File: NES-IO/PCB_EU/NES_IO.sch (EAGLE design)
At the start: 63 parts, among them IC1 74HC125D, J1.1 MY_JUMPER, J1.2 MY_JUMPER, J2.2 10k, J4.C MY_JUMPER, J4.V MY_JUMPER, J6 MY_JUMPER, J7 MY_JUMPER

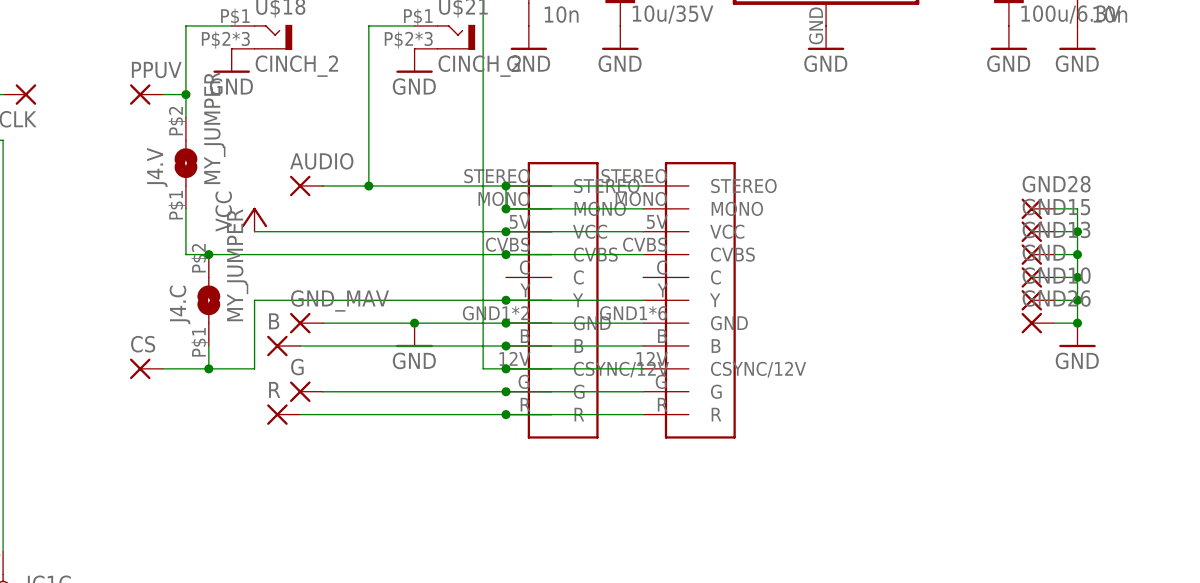
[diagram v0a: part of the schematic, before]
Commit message: Common design for MultiAV (from SNES or GC) and FR-NES-RGB jack
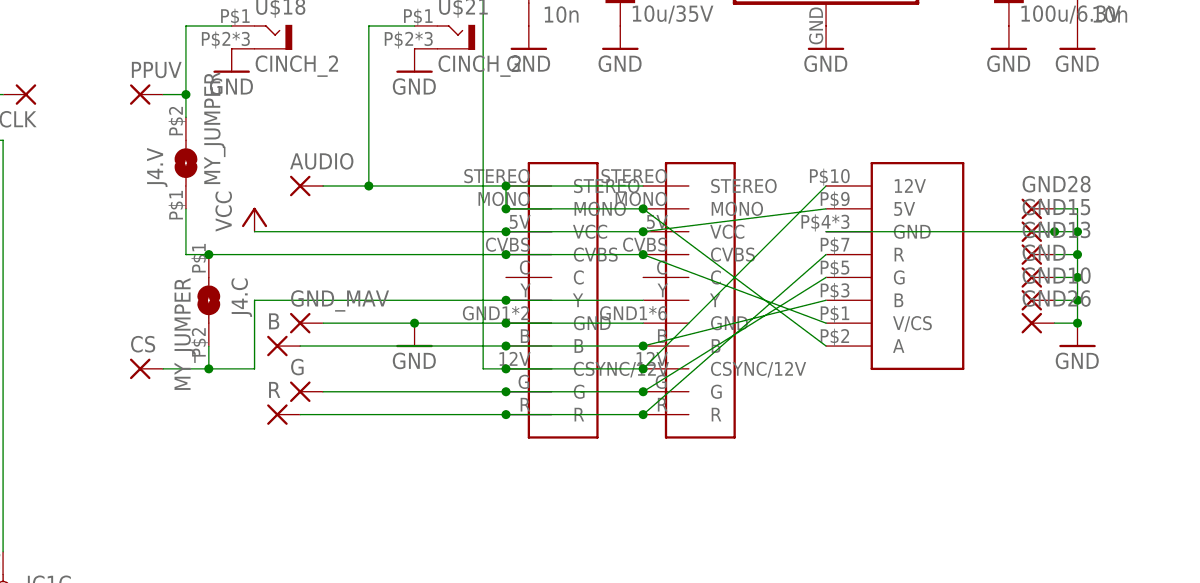
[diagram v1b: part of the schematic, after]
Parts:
- added U$8: NESFR_JACK2, nintendo:NESFR_JACK2
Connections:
- net DC2: now also U$8.12V
- net GND: now also U$8.GND
- net N$30: now also J4.C.1, U$8.V/CS; no longer J4.C.2
- net N$5: now also U$8.A
- net N$6: now also U$8.B
- net N$7: now also J4.C.2; no longer J4.C.1
- net N$8: now also U$8.G
- net N$9: now also U$8.R
- net VCC: now also U$8.5V
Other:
- moved on the sheet: J4.C
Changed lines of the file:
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@@
 <part name="GND16" library="supply1" deviceset="GND" device=""/>
 <part name="GND29" library="supply1" deviceset="GND" device=""/>
+<part name="U$8" library="nintendo" deviceset="NESFR_JACK2" device=""/>
 </parts>
 <sheets>
@@
 <instance part="GND11" gate="1" x="109.22" y="81.28"/>
 <instance part="GND_MAV" gate="1" x="22.86" y="83.82"/>
-<instance part="J4.C" gate="G$1" x="12.7" y="86.36" rot="R90"/>
+<instance part="J4.C" gate="G$1" x="12.7" y="86.36" rot="R270"/>
 <instance part="U$5" gate="G$1" x="-58.42" y="106.68"/>
 <instance part="U$5" gate="G$2" x="-58.42" y="132.08" rot="R90"/>
@@
 <instance part="GND16" gate="1" x="15.24" y="111.76"/>
 <instance part="GND29" gate="1" x="35.56" y="111.76"/>
+<instance part="U$8" gate="G$1" x="86.36" y="91.44"/>
 </instances>
 <busses>
@@
 <junction x="45.72" y="93.98"/>
 <pinref part="U$19" gate="G$1" pin="VCC"/>
+<pinref part="U$8" gate="G$1" pin="5V"/>
+<wire x1="60.96" y1="93.98" x2="81.28" y2="96.52" width="0.1524" layer="91"/>
+<junction x="60.96" y="93.98"/>
 </segment>
 <segment>
@@
 <wire x1="106.68" y1="93.98" x2="109.22" y2="93.98" width="0.1524" layer="91"/>
 <junction x="109.22" y="93.98"/>
+<pinref part="U$8" gate="G$1" pin="GND"/>
+<wire x1="81.28" y1="93.98" x2="106.68" y2="93.98" width="0.1524" layer="91"/>
+<junction x="106.68" y="93.98"/>
 </segment>
 <segment>
@@
 <junction x="45.72" y="78.74"/>
 <pinref part="U$19" gate="G$1" pin="CSYNC/12V"/>
+<pinref part="U$8" gate="G$1" pin="12V"/>
+<wire x1="81.28" y1="99.06" x2="60.96" y2="78.74" width="0.1524" layer="91"/>
+<junction x="60.96" y="78.74"/>
 </segment>
 </net>
@@
 <pinref part="U$21" gate="G$1" pin="T"/>
 <wire x1="35.56" y1="116.84" x2="30.48" y2="116.84" width="0.1524" layer="91"/>
+<pinref part="U$8" gate="G$1" pin="A"/>
+<wire x1="81.28" y1="81.28" x2="60.96" y2="96.52" width="0.1524" layer="91"/>
+<junction x="60.96" y="96.52"/>
 </segment>
 </net>
@@
 <junction x="45.72" y="81.28"/>
 <pinref part="U$19" gate="G$1" pin="B"/>
+<pinref part="U$8" gate="G$1" pin="B"/>
+<wire x1="81.28" y1="86.36" x2="60.96" y2="81.28" width="0.1524" layer="91"/>
+<junction x="60.96" y="81.28"/>
 </segment>
 </net>
@@
 <wire x1="45.72" y1="86.36" x2="17.78" y2="86.36" width="0.1524" layer="91"/>
 <wire x1="17.78" y1="86.36" x2="17.78" y2="78.74" width="0.1524" layer="91"/>
-<pinref part="J4.C" gate="G$1" pin="1"/>
-<wire x1="12.7" y1="81.28" x2="12.7" y2="78.74" width="0.1524" layer="91"/>
-<junction x="12.7" y="78.74"/>
 <pinref part="U$20" gate="G$1" pin="Y"/>
 <junction x="45.72" y="86.36"/>
 <pinref part="U$19" gate="G$1" pin="Y"/>
+<pinref part="J4.C" gate="G$1" pin="2"/>
+<wire x1="12.7" y1="78.74" x2="12.7" y2="81.28" width="0.1524" layer="91"/>
+<junction x="12.7" y="78.74"/>
 </segment>
 </net>
@@
 <junction x="45.72" y="76.2"/>
 <pinref part="U$19" gate="G$1" pin="G"/>
+<pinref part="U$8" gate="G$1" pin="G"/>
+<wire x1="81.28" y1="88.9" x2="60.96" y2="76.2" width="0.1524" layer="91"/>
+<junction x="60.96" y="76.2"/>
 </segment>
 </net>
@@
 <junction x="45.72" y="73.66"/>
 <pinref part="U$19" gate="G$1" pin="R"/>
+<pinref part="U$8" gate="G$1" pin="R"/>
+<wire x1="81.28" y1="91.44" x2="60.96" y2="73.66" width="0.1524" layer="91"/>
+<junction x="60.96" y="73.66"/>
 </segment>
 </net>
@@
 <net name="N$30" class="0">
 <segment>
-<pinref part="J4.C" gate="G$1" pin="2"/>
 <wire x1="12.7" y1="91.44" x2="45.72" y2="91.44" width="0.1524" layer="91"/>
 <wire x1="45.72" y1="91.44" x2="60.96" y2="91.44" width="0.1524" layer="91"/>
-<wire x1="12.7" y1="91.44" x2="10.16" y2="91.44" width="0.1524" layer="91"/>
-<junction x="12.7" y="91.44"/>
 <pinref part="U$20" gate="G$1" pin="CVBS"/>
 <junction x="45.72" y="91.44"/>
 <pinref part="U$19" gate="G$1" pin="CVBS"/>
 <pinref part="J4.V" gate="G$1" pin="1"/>
+<junction x="60.96" y="91.44"/>
+<pinref part="U$8" gate="G$1" pin="V/CS"/>
 <wire x1="10.16" y1="91.44" x2="10.16" y2="96.52" width="0.1524" layer="91"/>
-</segment>
-</net>
+<wire x1="81.28" y1="83.82" x2="60.96" y2="91.44" width="0.1524" layer="91"/>
+<wire x1="10.16" y1="91.44" x2="12.7" y2="91.44" width="0.1524" layer="91"/>
+<pinref part="J4.C" gate="G$1" pin="1"/>
+<junction x="12.7" y="91.44"/>
+</segment>
+</net>
